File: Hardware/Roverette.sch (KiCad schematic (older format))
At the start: 36 parts, among them SW1 SW_Push, U1 ESP32-WROOM-32U, U2 DRV8874

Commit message: Add files via upload
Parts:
- removed U2: DRV8874, Package_SO:HTSSOP-16-1EP_4.4x5mm_P0.65mm_EP3.4x5mm_Mask3x3mm_ThermalVias, symbol Driver_Motor:DRV8874
- removed U?: LM2596S-3.3, Package_TO_SOT_SMD:TO-263-5_TabPin3, symbol Regulator_Switching:LM2596S-3.3
- added D?: GREEN, symbol Device:LED_Small
- added R?: 4.7k, Resistor_SMD:R_0805_2012Metric, symbol Device:R_Small_US
- added U?: DRV8874, Package_SO:HTSSOP-16-1EP_4.4x5mm_P0.65mm_EP3.4x5mm_Mask3x3mm_ThermalVias, symbol Driver_Motor:DRV8874
- added U?: TPS56628, Package_SO:HSOP-8-1EP_3.9x4.9mm_P1.27mm_EP2.41x3.1mm_ThermalVias, symbol Power_Management:TPS56628
- D1: value 2A -> 5A
- L2: Idc (none) -> 5A
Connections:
- net labels removed: ADR, FSYNC, INT
- wire segments 98 -> 106
- no-connect marks 17 -> 27
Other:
- note removed: "2A"
- moved on the sheet: C10, C11, C12, C13, C14, C9, D1, L2, R4, R5, R6, SW1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

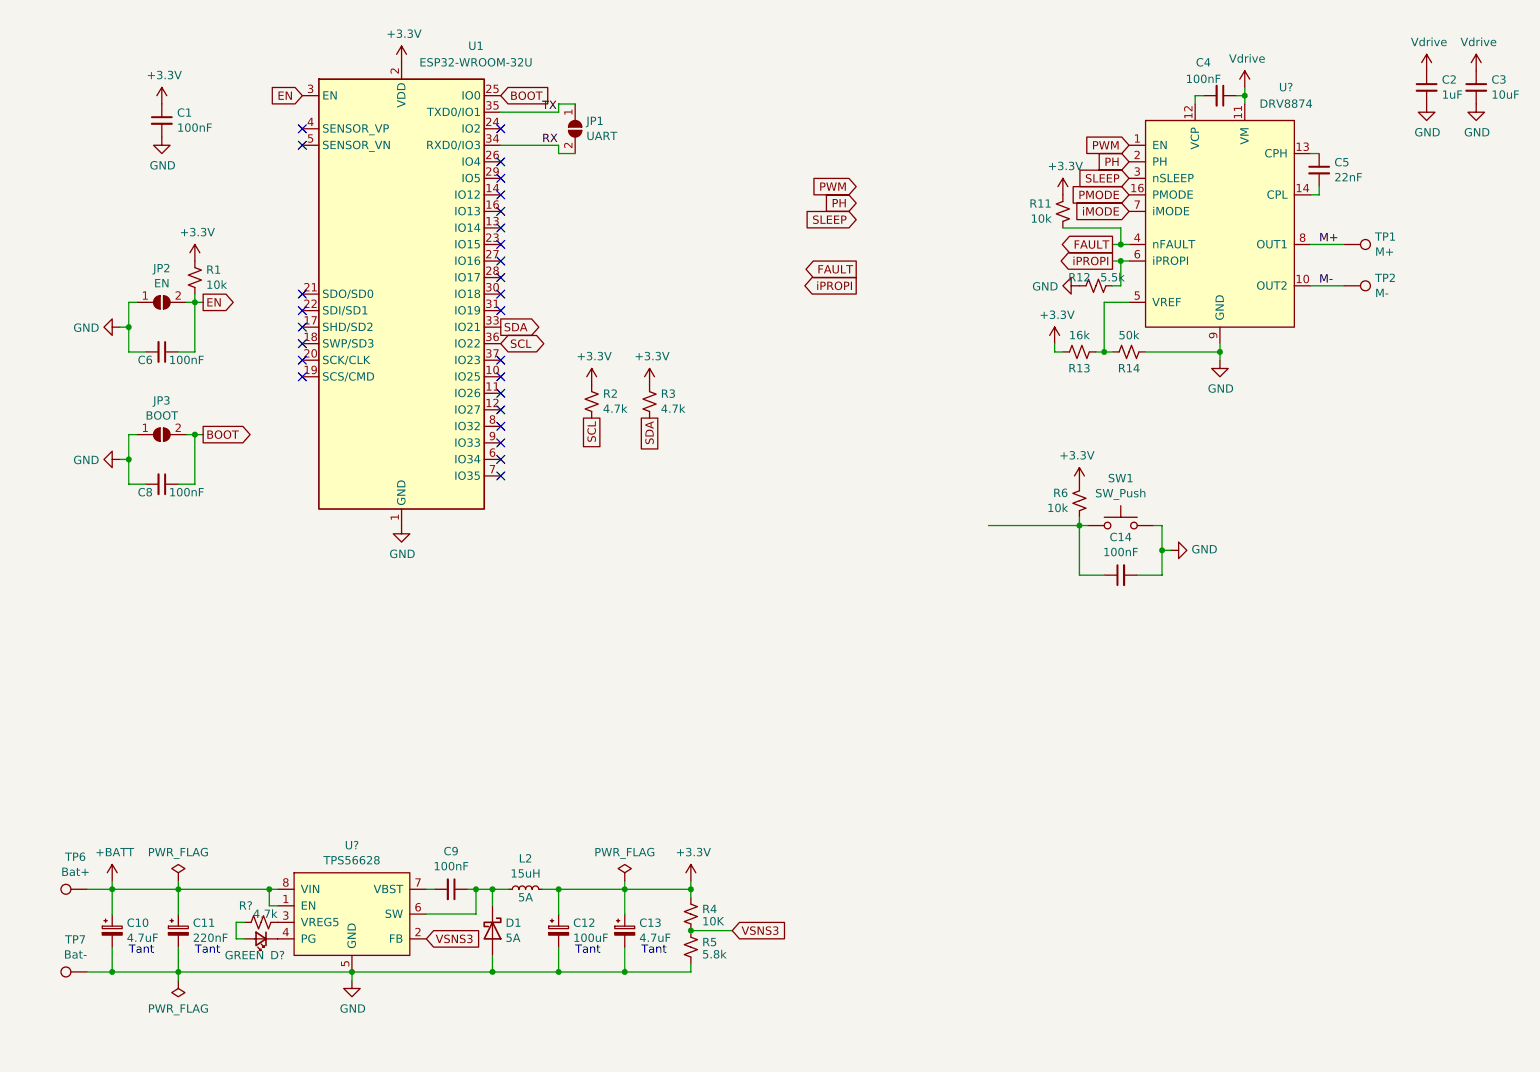
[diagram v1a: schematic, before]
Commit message: Test pads changed to push buttons, DMM test point added for measuring current Signed-off-by: Usman <usmanmehmood55@gmail.com>
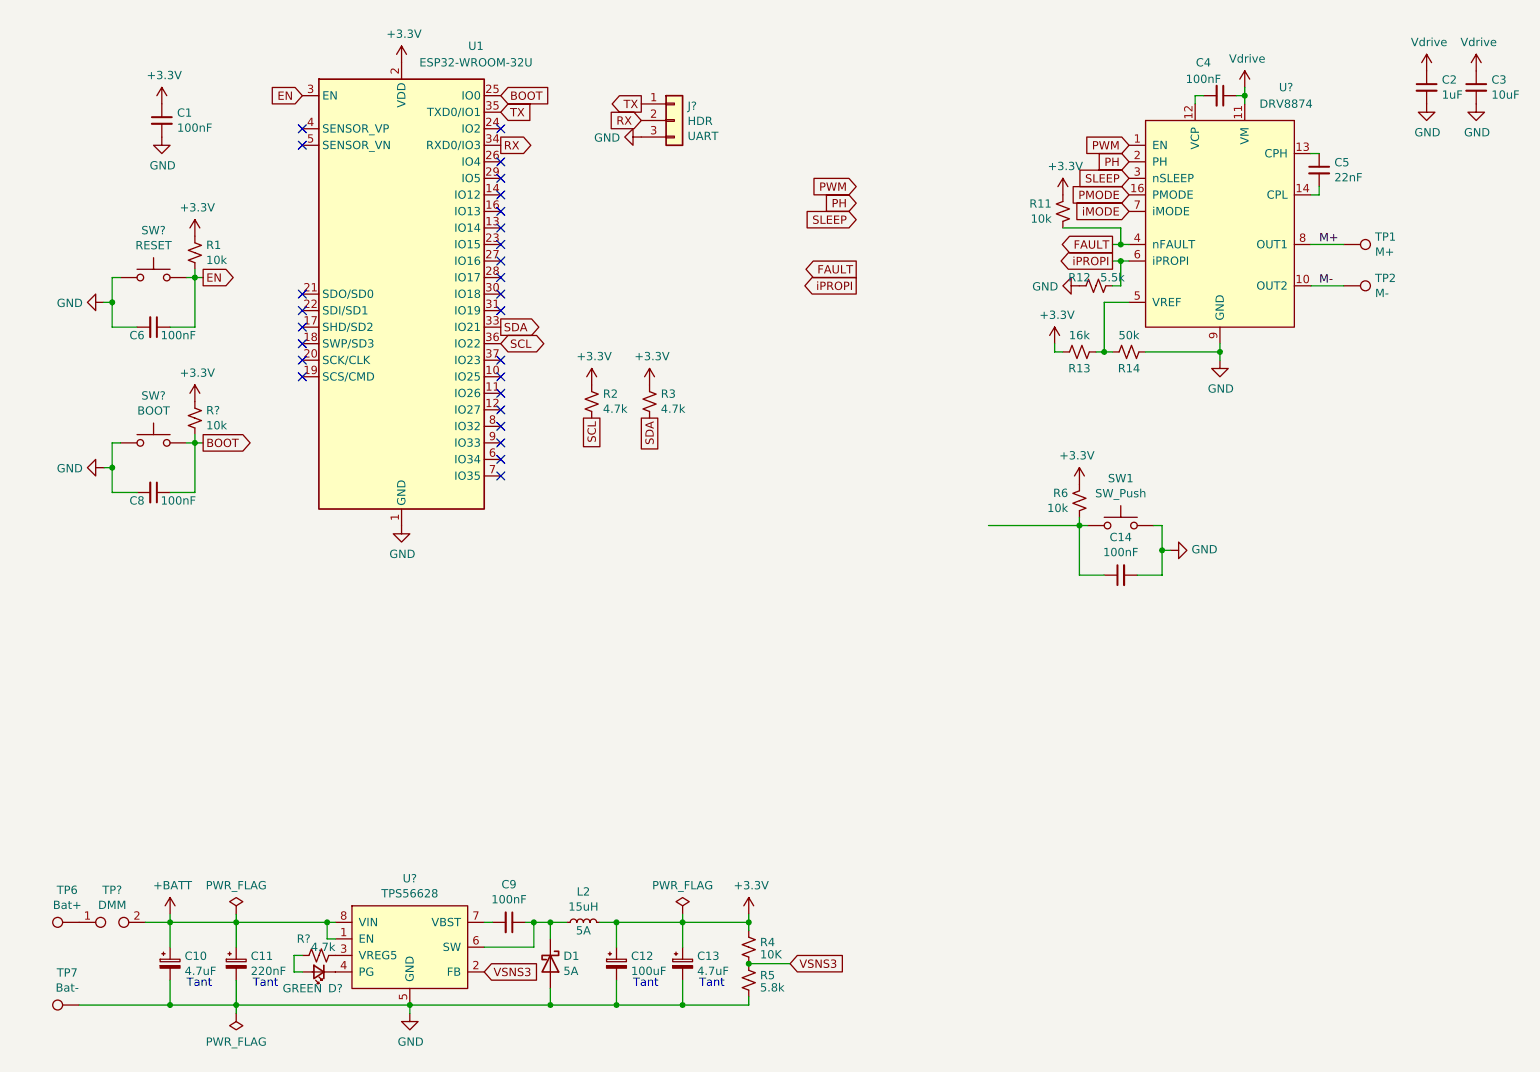
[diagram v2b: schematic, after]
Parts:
- removed JP1: UART, Jumper:SolderJumper-2_P1.3mm_Open_Pad1.0x1.5mm, symbol Jumper:SolderJumper_2_Open
- removed JP2: EN, Jumper:SolderJumper-2_P1.3mm_Open_Pad1.0x1.5mm, symbol Jumper:SolderJumper_2_Open
- removed JP3: BOOT, Jumper:SolderJumper-2_P1.3mm_Open_Pad1.0x1.5mm, symbol Jumper:SolderJumper_2_Open
- added J?: HDR, symbol Connector_Generic:Conn_01x03
- added R?: 10k, Resistor_SMD:R_0805_2012Metric, symbol Device:R_Small_US
- added SW? (x2): SW_Push, Button_Switch_SMD:SW_SPST_CK_RS282G05A3, symbol Switch:SW_Push
- added TP?: TestPoint_2Pole, symbol Connector:TestPoint_2Pole
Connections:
- net +3V3: now also R?.1
- net +BATT: now also TP?.2; no longer TP6.1
- net BOOT: now also R?.2, SW?.2
- net EN: now also SW?.2
- net GND: now also J?.3 (Pin_3), SW?.1, SW?.1
- net RX: now also J?.2 (Pin_2)
- net TX: now also J?.1 (Pin_1)
- new net: TP6.1, TP?.1
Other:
- moved on the sheet: C10, C11, C12, C13, C6, C8, C9, D1, D?, L2, R1, R4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

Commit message: Added footprint
Signed-off-by: Usman <usmanmehmood55@gmail.com>
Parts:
- TP?: footprint (none) -> TestPoint:TestPoint_2Pads_Pitch2.54mm_Drill0.8mm
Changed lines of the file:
@@
 F 0 "TP?" H 1700 6695 50  0000 C CNN
 F 1 "TestPoint_2Pole" H 1700 6604 50  0001 C CNN
-F 2 "" H 1700 6500 50  0001 C CNN
+F 2 "TestPoint:TestPoint_2Pads_Pitch2.54mm_Drill0.8mm" H 1700 6500 50  0001 C CNN
 F 3 "~" H 1700 6500 50  0001 C CNN
 F 4 "DMM" H 1700 6604 50  0000 C CNN "Field4"

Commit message: Schematic updated
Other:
- note added: "To be replaced by ESP32 Cam"
- moved on the sheet: J?
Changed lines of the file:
@@
 NoConn ~ 4050 3500
 NoConn ~ 4050 3600
-Text GLabel 6200 2050 0    50   Input ~ 0
+Text GLabel 6300 2000 0    50   Input ~ 0
 PWM
-Text GLabel 6200 2150 0    50   Input ~ 0
+Text GLabel 6300 2100 0    50   Input ~ 0
 PH
-Text GLabel 6200 2250 0    50   Input ~ 0
+Text GLabel 6300 2200 0    50   Input ~ 0
 SLEEP
-Text GLabel 6200 2550 0    50   Output ~ 0
+Text GLabel 6300 2500 0    50   Output ~ 0
 FAULT
-Text GLabel 6200 2650 0    50   Output ~ 0
+Text GLabel 6300 2600 0    50   Output ~ 0
 iPROPI
 $Bitmap
@@
 L Connector_Generic:Conn_01x03 J?
 U 1 1 5FF13025
-P 5100 1650
-F 0 "J?" H 5180 1737 50  0000 L CNN
-F 1 "HDR" H 5180 1646 50  0000 L CNN
-F 2 "" H 5100 1650 50  0001 C CNN
-F 3 "~" H 5100 1650 50  0001 C CNN
-F 4 "UART" H 5180 1555 50  0000 L CNN "Field4"
-	1    5100 1650
+P 4900 2250
+F 0 "J?" H 4980 2337 50  0000 L CNN
+F 1 "HDR" H 4980 2246 50  0000 L CNN
+F 2 "" H 4900 2250 50  0001 C CNN
+F 3 "~" H 4900 2250 50  0001 C CNN
+F 4 "UART" H 4980 2155 50  0000 L CNN "Field4"
+	1    4900 2250
 	1    0    0    -1
 $EndComp
@@
 Text GLabel 4050 1600 2    50   Input ~ 0
 TX
-Text GLabel 4900 1650 0    50   Input ~ 0
+Text GLabel 4700 2250 0    50   Input ~ 0
 RX
-Text GLabel 4900 1550 0    50   Output ~ 0
+Text GLabel 4700 2150 0    50   Output ~ 0
 TX
 $Comp
 L power:GND #PWR?
 U 1 1 5FF3D9B5
-P 4900 1750
-F 0 "#PWR?" H 4900 1500 50  0001 C CNN
-F 1 "GND" V 4905 1622 50  0000 R CNN
-F 2 "" H 4900 1750 50  0001 C CNN
-F 3 "" H 4900 1750 50  0001 C CNN
-	1    4900 1750
+P 4700 2350
+F 0 "#PWR?" H 4700 2100 50  0001 C CNN
+F 1 "GND" V 4705 2222 50  0000 R CNN
+F 2 "" H 4700 2350 50  0001 C CNN
+F 3 "" H 4700 2350 50  0001 C CNN
+	1    4700 2350
 	0    1    1    0
 $EndComp
@@
 Wire Wire Line
 	1500 7000 2050 7000
+Wire Notes Line
+	1100 4650 1100 1000
+Wire Notes Line
+	1100 1000 5450 1000
+Wire Notes Line
+	5450 1000 5450 4650
+Wire Notes Line
+	1100 4650 5450 4650
+Text Notes 4200 4600 0    50   ~ 0
+To be replaced by ESP32 Cam
 $EndSCHEMATC
